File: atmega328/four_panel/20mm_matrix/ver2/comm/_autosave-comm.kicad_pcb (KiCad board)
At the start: 2 copper layers, 40 x 40 mm, 14 parts, among them IC5 ATMEGA328-A, M1 CONN_1, M2 CONN_1, P1 CONN15, P2 CONN15, P4 CONN_2X2, P5 CONN_2X2, P6 CONN_2X2, P7 CONN_2X2, P8 CONN_2, X5 CER_RESO

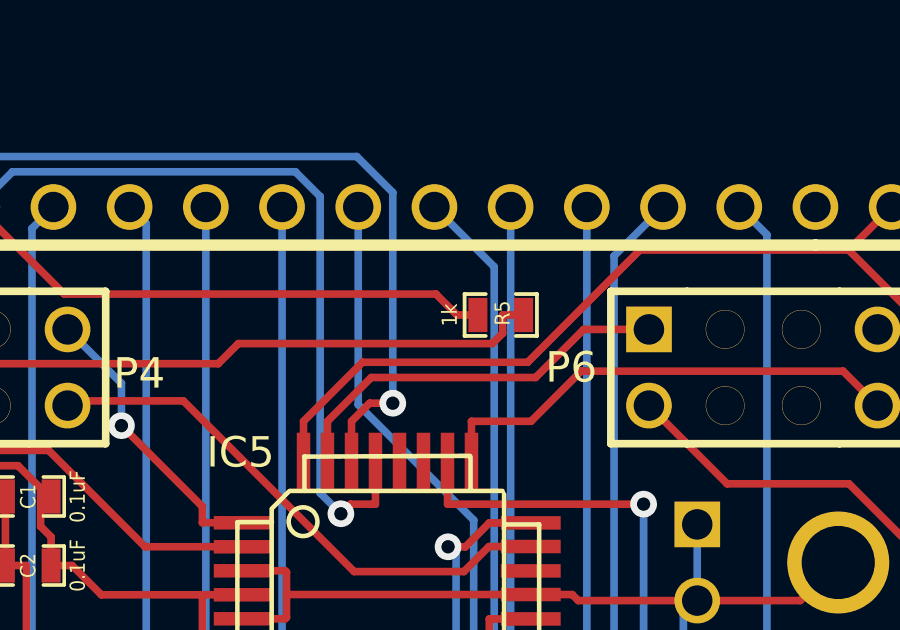
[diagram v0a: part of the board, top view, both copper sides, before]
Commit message: Modified BOM for both comm and driver PCBs.
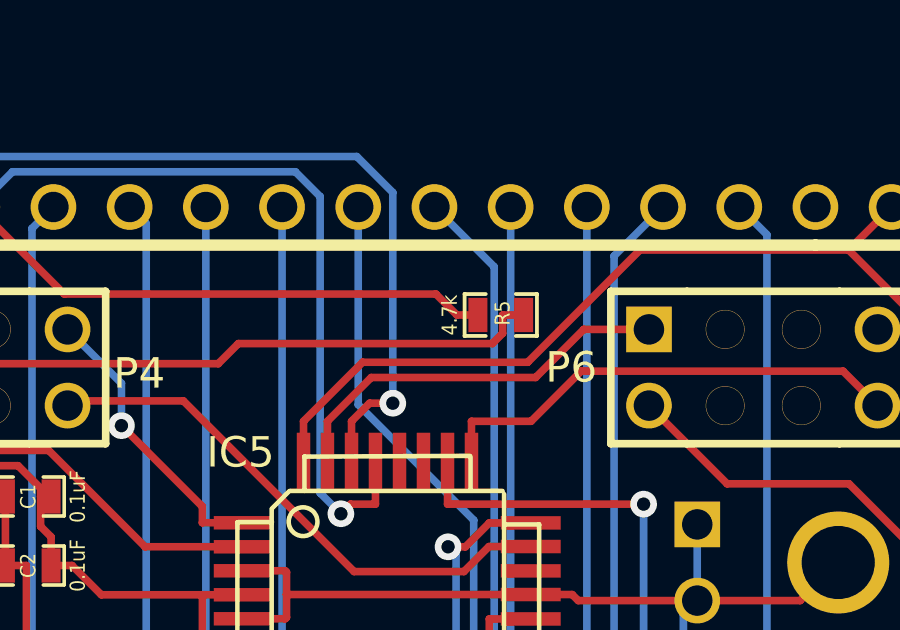
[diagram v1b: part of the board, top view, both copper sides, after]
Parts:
- R5: value 1k -> 4.7k
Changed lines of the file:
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@@
     (links 53)
     (no_connects 0)
-    (area 48.5244 49.577499 90.9676 90.424501)
+    (area 48.5244 49.577499 90.125001 90.424501)
     (thickness 1.6)
     (drawings 7)
@@
       (drillshape 0)
       (scaleselection 1)
-      (outputdirectory gerber_v0p2/))
+      (outputdirectory gerber_v0p2_r1/))
   )
   (net 0 "")
@@
       (effects (font (size 0.50038 0.4572) (thickness 0.1143)))
     )
-    (fp_text value 1k (at -1.69926 0 90) (layer F.SilkS)
+    (fp_text value 4.7k (at -1.69926 0 90) (layer F.SilkS)
       (effects (font (size 0.508 0.4572) (thickness 0.1143)))
     )
